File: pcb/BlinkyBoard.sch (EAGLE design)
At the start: 26 parts, among them Q1 16 MHz

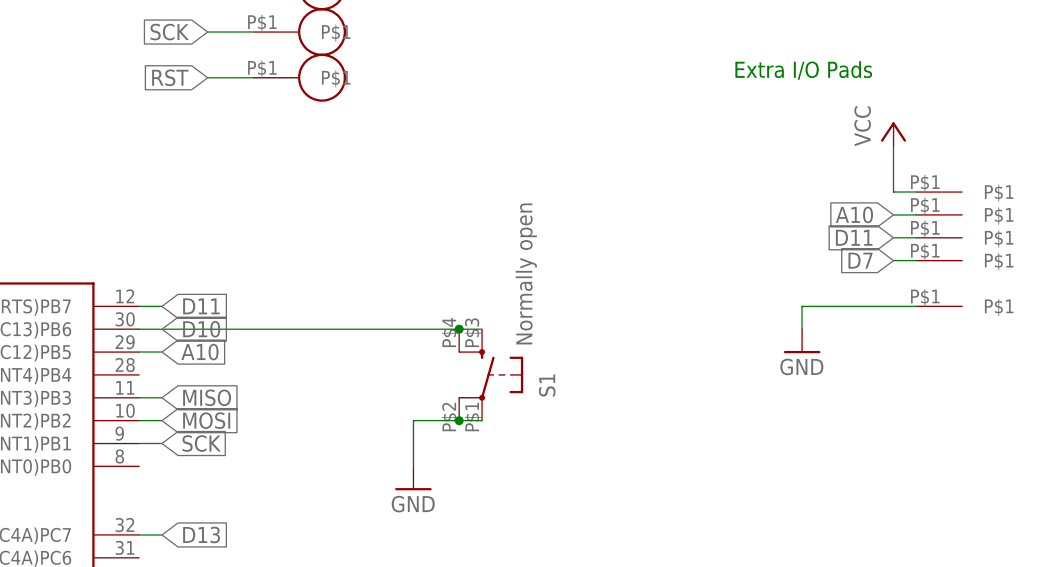
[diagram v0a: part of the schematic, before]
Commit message: Fix label: Analog input is actually on A9, not 11!
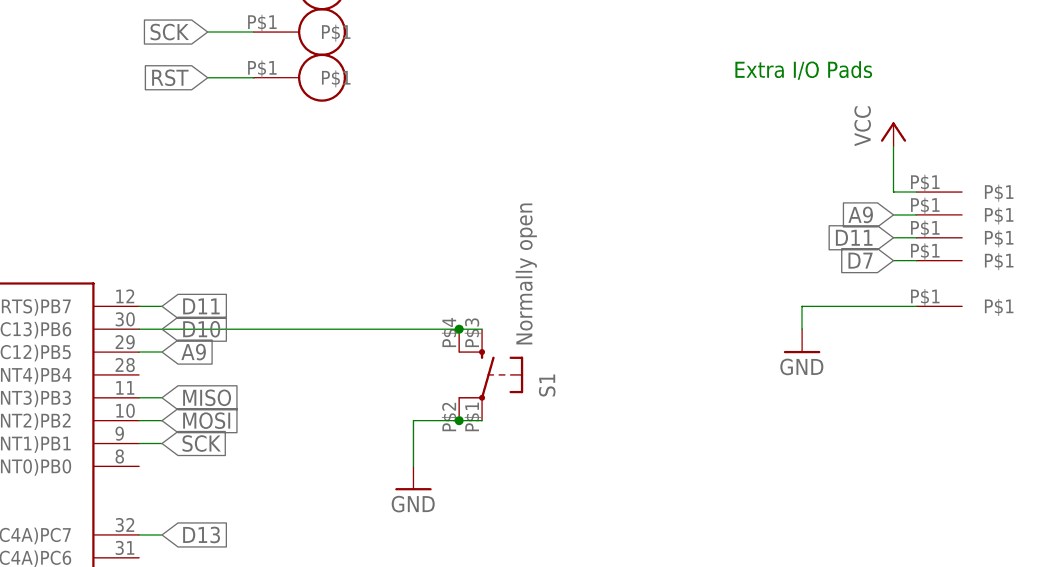
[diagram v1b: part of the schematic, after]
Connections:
- net A10 renamed A9
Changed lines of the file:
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@@
 </segment>
 </net>
-<net name="A10" class="0">
+<net name="A9" class="0">
 <segment>
 <pinref part="U$2" gate="G$1" pin="(PCINT5/OC1A/#OC4B/ADC12)PB5"/>
